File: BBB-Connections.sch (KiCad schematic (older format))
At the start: 9 parts

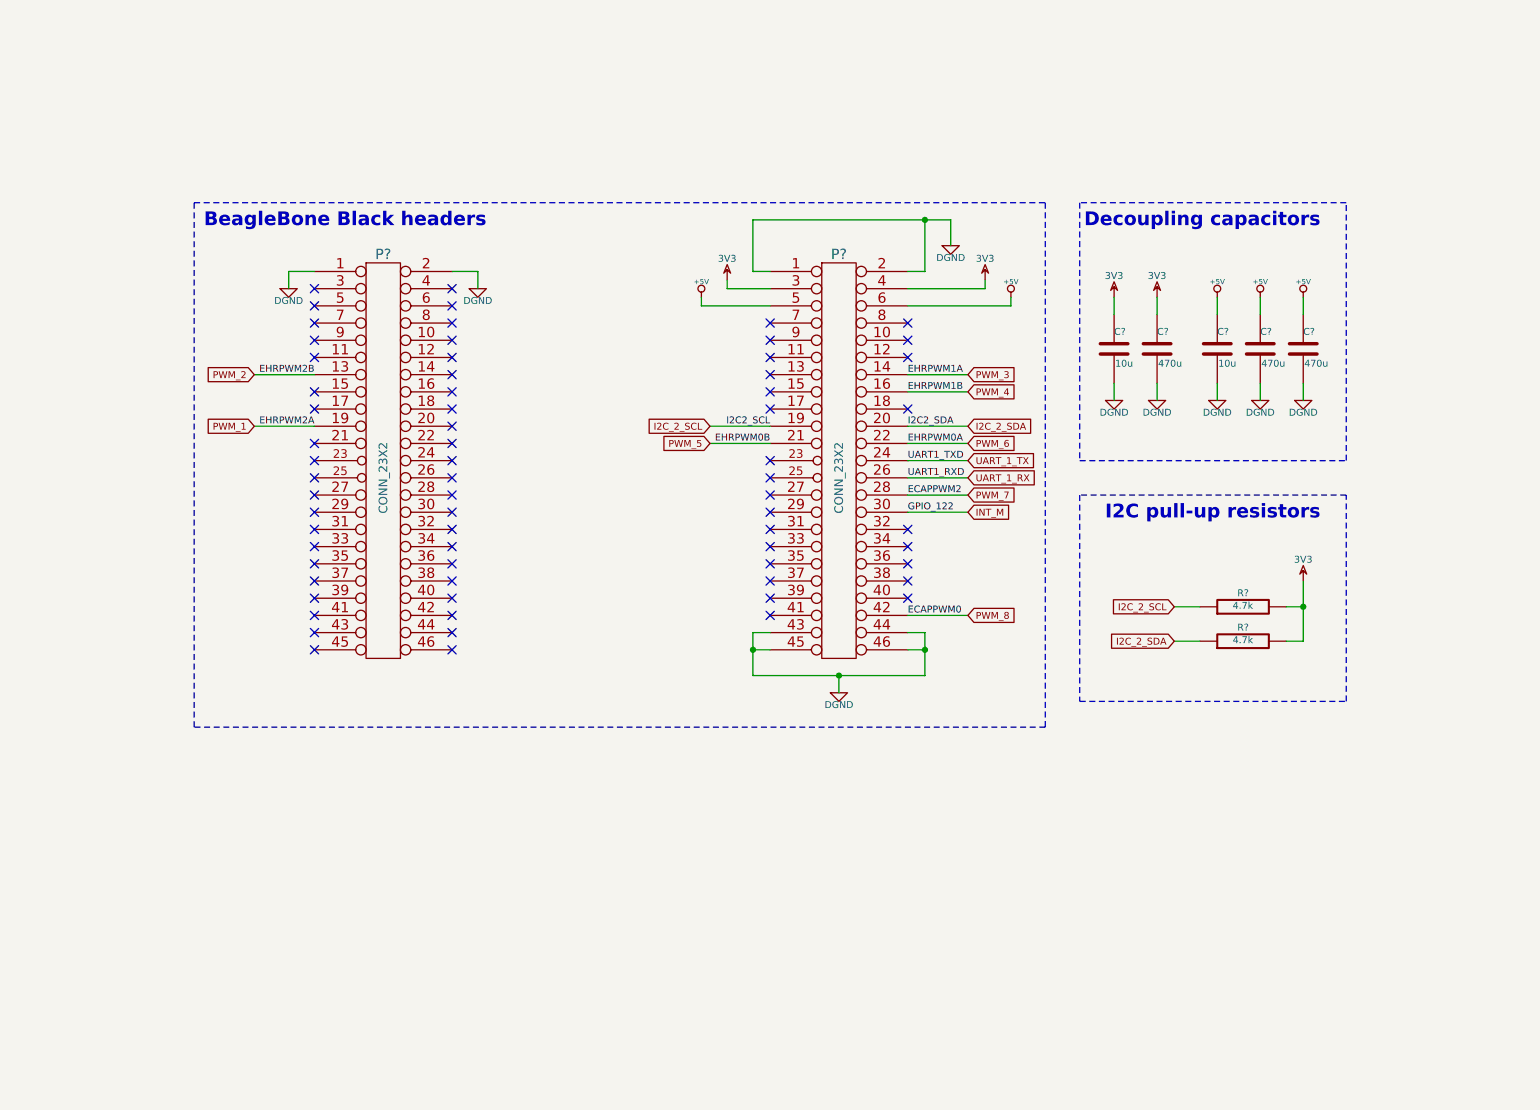
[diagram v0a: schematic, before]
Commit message: added bat mgmt, pwr select, xbee header
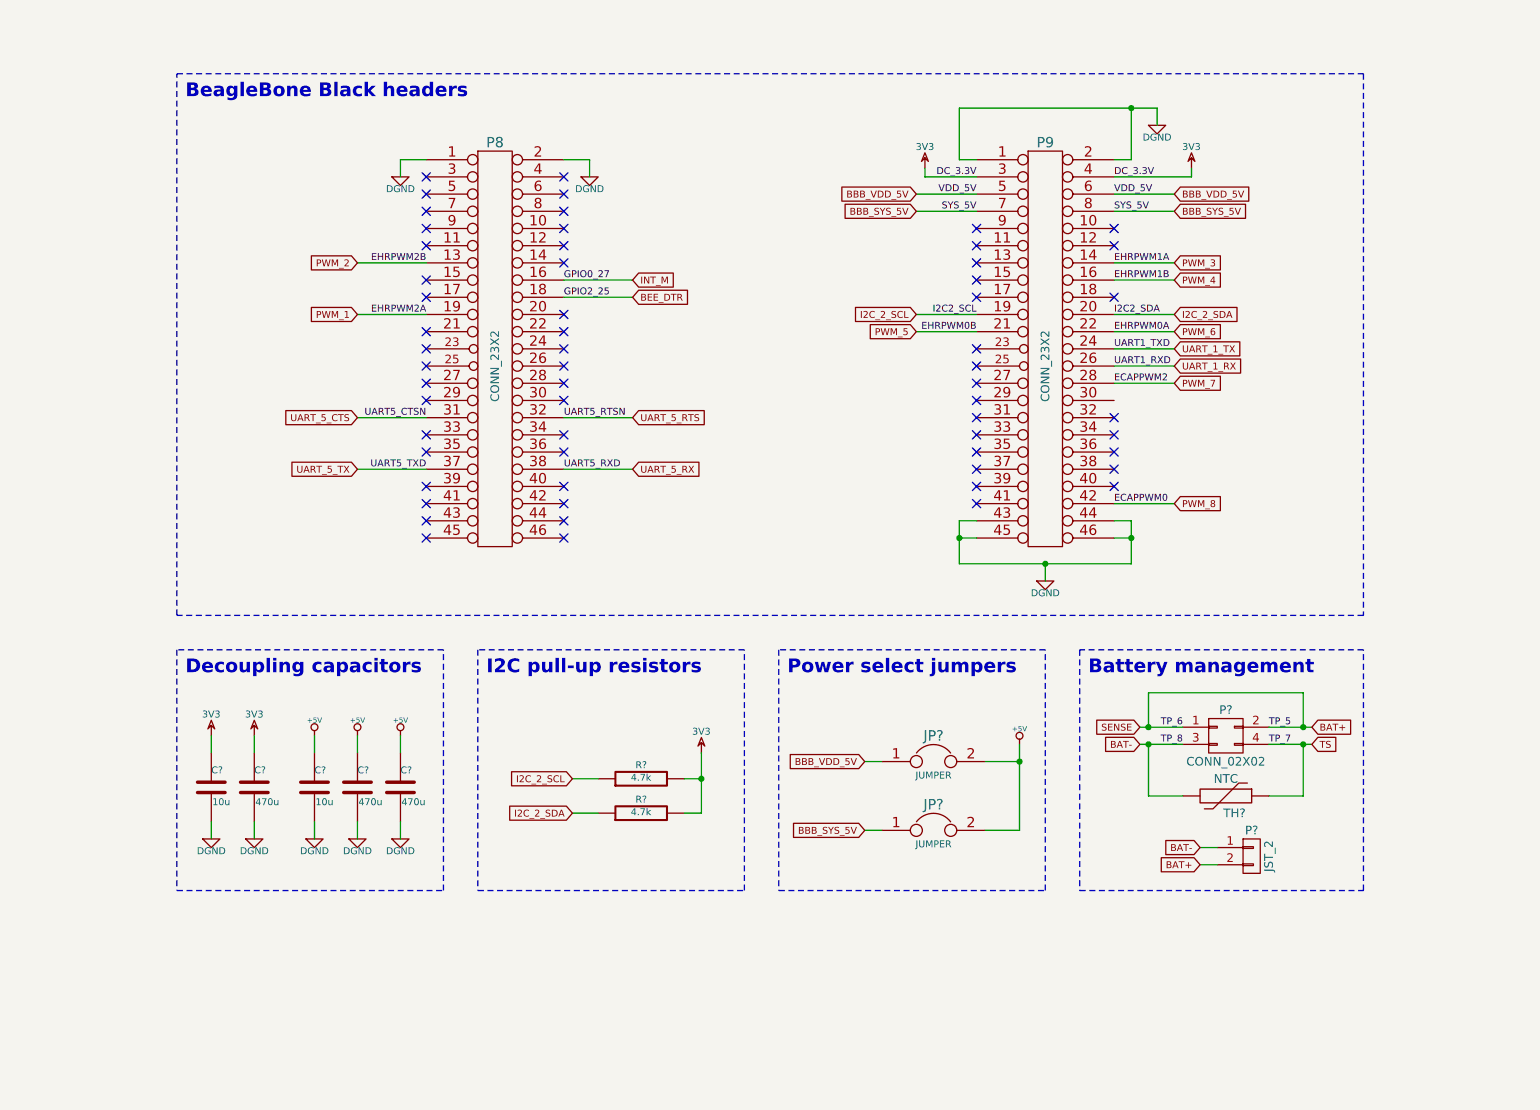
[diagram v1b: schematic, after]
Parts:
- added JP? (x2): JUMPER, symbol JUMPER
- added P?: CONN_02X02, symbol CONN_02X02
- added P?: JST_2, symbol JST_2
- added TH?: NTC, symbol NTC
- gave numbers to parts that had none: 2
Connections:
- net +5V: now also JP?.2, JP?.2; no longer P9.5 (P5), P9.6 (P6)
- net INT_M: now also P8.16 (P16); no longer P9.30 (P30)
- net BBB_SYS_5V: now reaches P9.7 (P7)
- net BBB_SYS_5V: now also P9.8 (P8), JP?.1
- net BEE_DTR: now reaches P8.18 (P18)
- net UART_5_CTS: now reaches P8.31 (P31)
- net UART_5_RTS: now reaches P8.32 (P32)
- net UART_5_TX: now reaches P8.37 (P37)
- net UART_5_RX: now reaches P8.38 (P38)
- new net BAT+: P?.1 (P1), P?.2 (BAT+), P?.2 (P2)
- new net BAT-: P?.1 (BAT-), P?.3 (P3), TH?.2
- new net BBB_VDD_5V: JP?.1, P9.5 (P5), P9.6 (P6)
- new net TS: P?.4 (P4), TH?.1
- no-connect marks 67 -> 59
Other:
- note added: "Battery management"
- note added: "Power select jumpers"
- moved on the sheet: C?, P8, P9, R?

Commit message: .sch done, .net done, components on PCB done
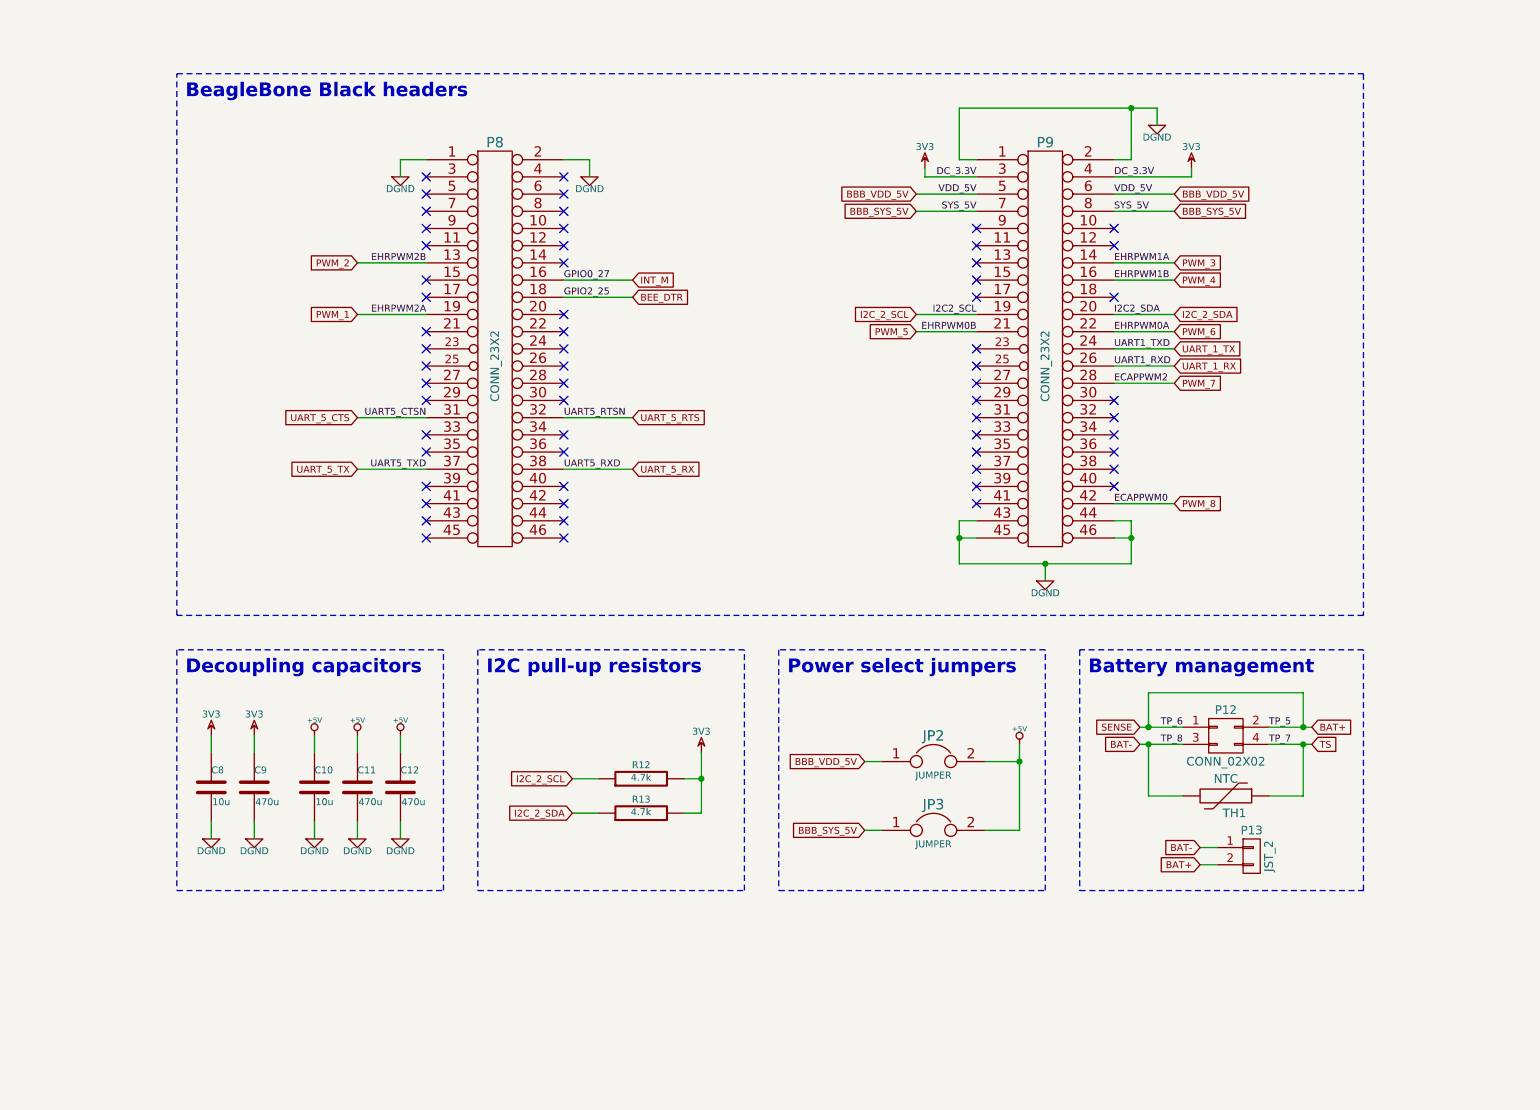
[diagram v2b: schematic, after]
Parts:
- gave numbers to parts that had none: 12
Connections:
- no-connect marks 59 -> 60
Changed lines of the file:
@@
 LIBS:contrib
 LIBS:valves
-LIBS:_dips-s
 LIBS:_memory
-LIBS:_power
 LIBS:_sensors
 LIBS:_xbee
@@
 UART_1_TX
 $Comp
-L R R?
+L R R12
 U 1 1 5429DC9D
 P 5050 5350
-F 0 "R?" V 5130 5350 40  0000 C CNN
+F 0 "R12" V 5130 5350 40  0000 C CNN
 F 1 "4.7k" V 5057 5351 40  0000 C CNN
 F 2 "" V 4980 5350 30  0000 C CNN
@@
 $EndComp
 $Comp
-L R R?
+L R R13
 U 1 1 5429DD22
 P 5050 5550
-F 0 "R?" V 5130 5550 40  0000 C CNN
+F 0 "R13" V 5130 5550 40  0000 C CNN
 F 1 "4.7k" V 5057 5551 40  0000 C CNN
 F 2 "" V 4980 5550 30  0000 C CNN
@@
 I2C_2_SCL
 $Comp
-L C C?
+L C C8
 U 1 1 542A418A
 P 2550 5400
-F 0 "C?" H 2550 5500 40  0000 L CNN
+F 0 "C8" H 2550 5500 40  0000 L CNN
 F 1 "10u" H 2556 5315 40  0000 L CNN
 F 2 "" H 2588 5250 30  0000 C CNN
@@
 $EndComp
 $Comp
-L 3V3 #PWR?
+L 3V3 #PWR052
 U 1 1 542B4D57
 P 5400 5200
-F 0 "#PWR?" H 5400 5300 40  0001 C CNN
+F 0 "#PWR052" H 5400 5300 40  0001 C CNN
 F 1 "3V3" H 5400 5325 40  0000 C CNN
 F 2 "" H 5400 5200 40  0000 C CNN
@@
 $EndComp
 $Comp
-L 3V3 #PWR?
+L 3V3 #PWR053
 U 1 1 542B4D69
 P 2550 5100
-F 0 "#PWR?" H 2550 5200 40  0001 C CNN
+F 0 "#PWR053" H 2550 5200 40  0001 C CNN
 F 1 "3V3" H 2550 5225 40  0000 C CNN
 F 2 "" H 2550 5100 40  0000 C CNN
@@
 $EndComp
 $Comp
-L DGND #PWR?
+L DGND #PWR054
 U 1 1 542B4D76
 P 2550 5700
-F 0 "#PWR?" H 2550 5700 40  0001 C CNN
+F 0 "#PWR054" H 2550 5700 40  0001 C CNN
 F 1 "DGND" H 2550 5630 40  0000 C CNN
 F 2 "" H 2550 5700 40  0000 C CNN
@@
 $EndComp
 $Comp
-L 3V3 #PWR?
+L 3V3 #PWR055
 U 1 1 542B4E7C
 P 2800 5100
-F 0 "#PWR?" H 2800 5200 40  0001 C CNN
+F 0 "#PWR055" H 2800 5200 40  0001 C CNN
 F 1 "3V3" H 2800 5225 40  0000 C CNN
 F 2 "" H 2800 5100 40  0000 C CNN
@@
 $EndComp
 $Comp
-L DGND #PWR?
+L DGND #PWR056
 U 1 1 542B4E82
 P 2800 5700
-F 0 "#PWR?" H 2800 5700 40  0001 C CNN
+F 0 "#PWR056" H 2800 5700 40  0001 C CNN
 F 1 "DGND" H 2800 5630 40  0000 C CNN
 F 2 "" H 2800 5700 40  0000 C CNN
@@
 $EndComp
 $Comp
-L C C?
+L C C12
 U 1 1 542B4F9A
 P 3650 5400
-F 0 "C?" H 3650 5500 40  0000 L CNN
+F 0 "C12" H 3650 5500 40  0000 L CNN
 F 1 "470u" H 3656 5315 40  0000 L CNN
 F 2 "" H 3688 5250 30  0000 C CNN
@@
 $EndComp
 $Comp
-L DGND #PWR?
+L DGND #PWR057
 U 1 1 542B4FA8
 P 3650 5700
-F 0 "#PWR?" H 3650 5700 40  0001 C CNN
+F 0 "#PWR057" H 3650 5700 40  0001 C CNN
 F 1 "DGND" H 3650 5630 40  0000 C CNN
 F 2 "" H 3650 5700 40  0000 C CNN
@@
 $EndComp
 $Comp
-L +5V #PWR?
+L +5V #PWR058
 U 1 1 542B4FF9
 P 3650 5100
-F 0 "#PWR?" H 3650 5190 20  0001 C CNN
+F 0 "#PWR058" H 3650 5190 20  0001 C CNN
 F 1 "+5V" H 3650 5190 30  0000 C CNN
 F 2 "" H 3650 5100 40  0000 C CNN
@@
 $EndComp
 $Comp
-L DGND #PWR?
+L DGND #PWR059
 U 1 1 542B5224
 P 8050 1550
-F 0 "#PWR?" H 8050 1550 40  0001 C CNN
+F 0 "#PWR059" H 8050 1550 40  0001 C CNN
 F 1 "DGND" H 8050 1480 40  0000 C CNN
 F 2 "" H 8050 1550 40  0000 C CNN
@@
 $EndComp
 $Comp
-L 3V3 #PWR?
+L 3V3 #PWR060
 U 1 1 542B57DC
 P 6700 1800
-F 0 "#PWR?" H 6700 1900 40  0001 C CNN
+F 0 "#PWR060" H 6700 1900 40  0001 C CNN
 F 1 "3V3" H 6700 1925 40  0000 C CNN
 F 2 "" H 6700 1800 40  0000 C CNN
@@
 $EndComp
 $Comp
-L 3V3 #PWR?
+L 3V3 #PWR061
 U 1 1 542B5823
 P 8250 1800
-F 0 "#PWR?" H 8250 1900 40  0001 C CNN
+F 0 "#PWR061" H 8250 1900 40  0001 C CNN
 F 1 "3V3" H 8250 1925 40  0000 C CNN
 F 2 "" H 8250 1800 40  0000 C CNN
@@
 NoConn ~ 7800 2150
 $Comp
-L DGND #PWR?
+L DGND #PWR062
 U 1 1 542B59B4
 P 7400 4200
-F 0 "#PWR?" H 7400 4200 40  0001 C CNN
+F 0 "#PWR062" H 7400 4200 40  0001 C CNN
 F 1 "DGND" H 7400 4130 40  0000 C CNN
 F 2 "" H 7400 4200 40  0000 C CNN
@@
 $EndComp
 $Comp
-L DGND #PWR?
+L DGND #PWR063
 U 1 1 542B5CB6
 P 4750 1850
-F 0 "#PWR?" H 4750 1850 40  0001 C CNN
+F 0 "#PWR063" H 4750 1850 40  0001 C CNN
 F 1 "DGND" H 4750 1780 40  0000 C CNN
 F 2 "" H 4750 1850 40  0000 C CNN
@@
 $EndComp
 $Comp
-L DGND #PWR?
+L DGND #PWR064
 U 1 1 542B5CEC
 P 3650 1850
-F 0 "#PWR?" H 3650 1850 40  0001 C CNN
+F 0 "#PWR064" H 3650 1850 40  0001 C CNN
 F 1 "DGND" H 3650 1780 40  0000 C CNN
 F 2 "" H 3650 1850 40  0000 C CNN
@@
 	8050 1450 8050 1550
 Wire Wire Line
-	6900 1450 7900 1450
-Wire Wire Line
-	7900 1450 8050 1450
+	6900 1450 8050 1450
 Wire Wire Line
 	6900 1450 6900 1750
@@
 	7000 3950 6900 3950
 Wire Wire Line
-	6900 3850 6900 3950
-Wire Wire Line
-	6900 3950 6900 4100
-Wire Wire Line
-	6900 4100 7400 4100
-Wire Wire Line
-	7400 4100 7900 4100
+	6900 3850 6900 4100
+Wire Wire Line
+	6900 4100 7900 4100
 Wire Wire Line
 	7400 4100 7400 4200
 Wire Wire Line
-	7900 4100 7900 3950
-Wire Wire Line
-	7900 3950 7900 3850
+	7900 4100 7900 3850
 Wire Wire Line
 	7900 3950 7800 3950
@@
 	6650 2650 7000 2650
 Wire Wire Line
-	5400 5200 5400 5350
-Wire Wire Line
-	5400 5350 5400 5550
+	5400 5200 5400 5550
 Wire Wire Line
 	5400 5350 5300 5350
@@
 	5650 4600 4100 4600
 $Comp
-L C C?
+L C C11
 U 1 1 5473086E
 P 3400 5400
-F 0 "C?" H 3400 5500 40  0000 L CNN
+F 0 "C11" H 3400 5500 40  0000 L CNN
 F 1 "470u" H 3406 5315 40  0000 L CNN
 F 2 "" H 3438 5250 30  0000 C CNN
@@
 $EndComp
 $Comp
-L C C?
+L C C10
 U 1 1 54730893
 P 3150 5400
-F 0 "C?" H 3150 5500 40  0000 L CNN
+F 0 "C10" H 3150 5500 40  0000 L CNN
 F 1 "10u" H 3156 5315 40  0000 L CNN
 F 2 "" H 3188 5250 30  0000 C CNN
@@
 $EndComp
 $Comp
-L +5V #PWR?
+L +5V #PWR065
 U 1 1 54730953
 P 3400 5100
-F 0 "#PWR?" H 3400 5190 20  0001 C CNN
+F 0 "#PWR065" H 3400 5190 20  0001 C CNN
 F 1 "+5V" H 3400 5190 30  0000 C CNN
 F 2 "" H 3400 5100 40  0000 C CNN
@@
 $EndComp
 $Comp
-L +5V #PWR?
+L +5V #PWR066
 U 1 1 54730966
 P 3150 5100
-F 0 "#PWR?" H 3150 5190 20  0001 C CNN
+F 0 "#PWR066" H 3150 5190 20  0001 C CNN
 F 1 "+5V" H 3150 5190 30  0000 C CNN
 F 2 "" H 3150 5100 40  0000 C CNN
@@
 $EndComp
 $Comp
-L DGND #PWR?
+L DGND #PWR067
 U 1 1 54730979
 P 3400 5700
-F 0 "#PWR?" H 3400 5700 40  0001 C CNN
+F 0 "#PWR067" H 3400 5700 40  0001 C CNN
 F 1 "DGND" H 3400 5630 40  0000 C CNN
 F 2 "" H 3400 5700 40  0000 C CNN
@@
 $EndComp
 $Comp
-L DGND #PWR?
+L DGND #PWR068
 U 1 1 5473098C
 P 3150 5700
-F 0 "#PWR?" H 3150 5700 40  0001 C CNN
+F 0 "#PWR068" H 3150 5700 40  0001 C CNN
 F 1 "DGND" H 3150 5630 40  0000 C CNN
 F 2 "" H 3150 5700 40  0000 C CNN
@@
 	3400 5100 3400 5200
 $Comp
-L C C?
+L C C9
 U 1 1 54730AD9
 P 2800 5400
-F 0 "C?" H 2800 5500 40  0000 L CNN
+F 0 "C9" H 2800 5500 40  0000 L CNN
 F 1 "470u" H 2806 5315 40  0000 L CNN
 F 2 "" H 2838 5250 30  0000 C CNN
@@
 BBB_VDD_5V
 $Comp
-L +5V #PWR?
+L +5V #PWR069
 U 1 1 54736B53
 P 7250 5150
-F 0 "#PWR?" H 7250 5240 20  0001 C CNN
+F 0 "#PWR069" H 7250 5240 20  0001 C CNN
 F 1 "+5V" H 7250 5240 30  0000 C CNN
 F 2 "" H 7250 5150 60  0000 C CNN
@@
 $EndComp
 $Comp
-L JUMPER JP?
+L JUMPER JP3
 U 1 1 54736B67
 P 6750 5650
-F 0 "JP?" H 6750 5800 60  0000 C CNN
+F 0 "JP3" H 6750 5800 60  0000 C CNN
 F 1 "JUMPER" H 6750 5570 40  0000 C CNN
 F 2 "" H 6750 5650 60  0000 C CNN
@@
 $EndComp
 $Comp
-L JUMPER JP?
+L JUMPER JP2
 U 1 1 54736BC2
 P 6750 5250
-F 0 "JP?" H 6750 5400 60  0000 C CNN
+F 0 "JP2" H 6750 5400 60  0000 C CNN
 F 1 "JUMPER" H 6750 5170 40  0000 C CNN
 F 2 "" H 6750 5250 60  0000 C CNN
@@
 $EndComp
 Wire Wire Line
-	7250 5150 7250 5250
-Wire Wire Line
-	7250 5250 7250 5650
+	7250 5150 7250 5650
 Wire Wire Line
 	7250 5250 7050 5250
@@
 	7400 4600 5850 4600
 $Comp
-L CONN_02X02 P?
+L CONN_02X02 P12
 U 1 1 547397DB
 P 8450 5100
-F 0 "P?" H 8450 5250 50  0000 C CNN
+F 0 "P12" H 8450 5250 50  0000 C CNN
 F 1 "CONN_02X02" H 8450 4950 50  0000 C CNN
 F 2 "" H 8450 3900 60  0000 C CNN
@@
 BAT+
 Wire Wire Line
-	8700 5050 8900 5050
-Wire Wire Line
-	8900 5050 8950 5050
+	8700 5050 8950 5050
 Text GLabel 7950 5150 0    40   Input ~ 0
 BAT-
 Wire Wire Line
-	7950 5150 8000 5150
-Wire Wire Line
-	8000 5150 8200 5150
-$Comp
-L JST_2 P?
+	7950 5150 8200 5150
+$Comp
+L JST_2 P13
 U 1 1 54739C03
 P 8600 5800
-F 0 "P?" H 8600 5950 50  0000 C CNN
+F 0 "P13" H 8600 5950 50  0000 C CNN
 F 1 "JST_2" V 8700 5800 50  0000 C CNN
 F 2 "" H 8600 5800 60  0000 C CNN
@@
 	8300 5850 8400 5850
 Wire Wire Line
-	7950 5050 8000 5050
-Wire Wire Line
-	8000 5050 8200 5050
+	7950 5050 8200 5050
 Wire Wire Line
 	8000 5050 8000 4850
@@
 Connection ~ 8900 5050
 $Comp
-L NTC TH?
+L NTC TH1
 U 1 1 5473A0B2
 P 8450 5450
-F 0 "TH?" V 8550 5500 50  0000 C CNN
+F 0 "TH1" V 8550 5500 50  0000 C CNN
 F 1 "NTC" V 8350 5450 50  0000 C CNN
 F 2 "" H 8450 5450 60  0000 C CNN
@@
 	8900 5450 8900 5150
 Wire Wire Line
-	8700 5150 8900 5150
-Wire Wire Line
-	8900 5150 8950 5150
+	8700 5150 8950 5150
 Text GLabel 8950 5150 2    40   Input ~ 0
 TS
@@
 Wire Notes Line
 	9250 4600 7600 4600
+NoConn ~ 7800 3150
 $EndSCHEMATC
